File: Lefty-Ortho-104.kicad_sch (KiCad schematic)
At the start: 11 parts

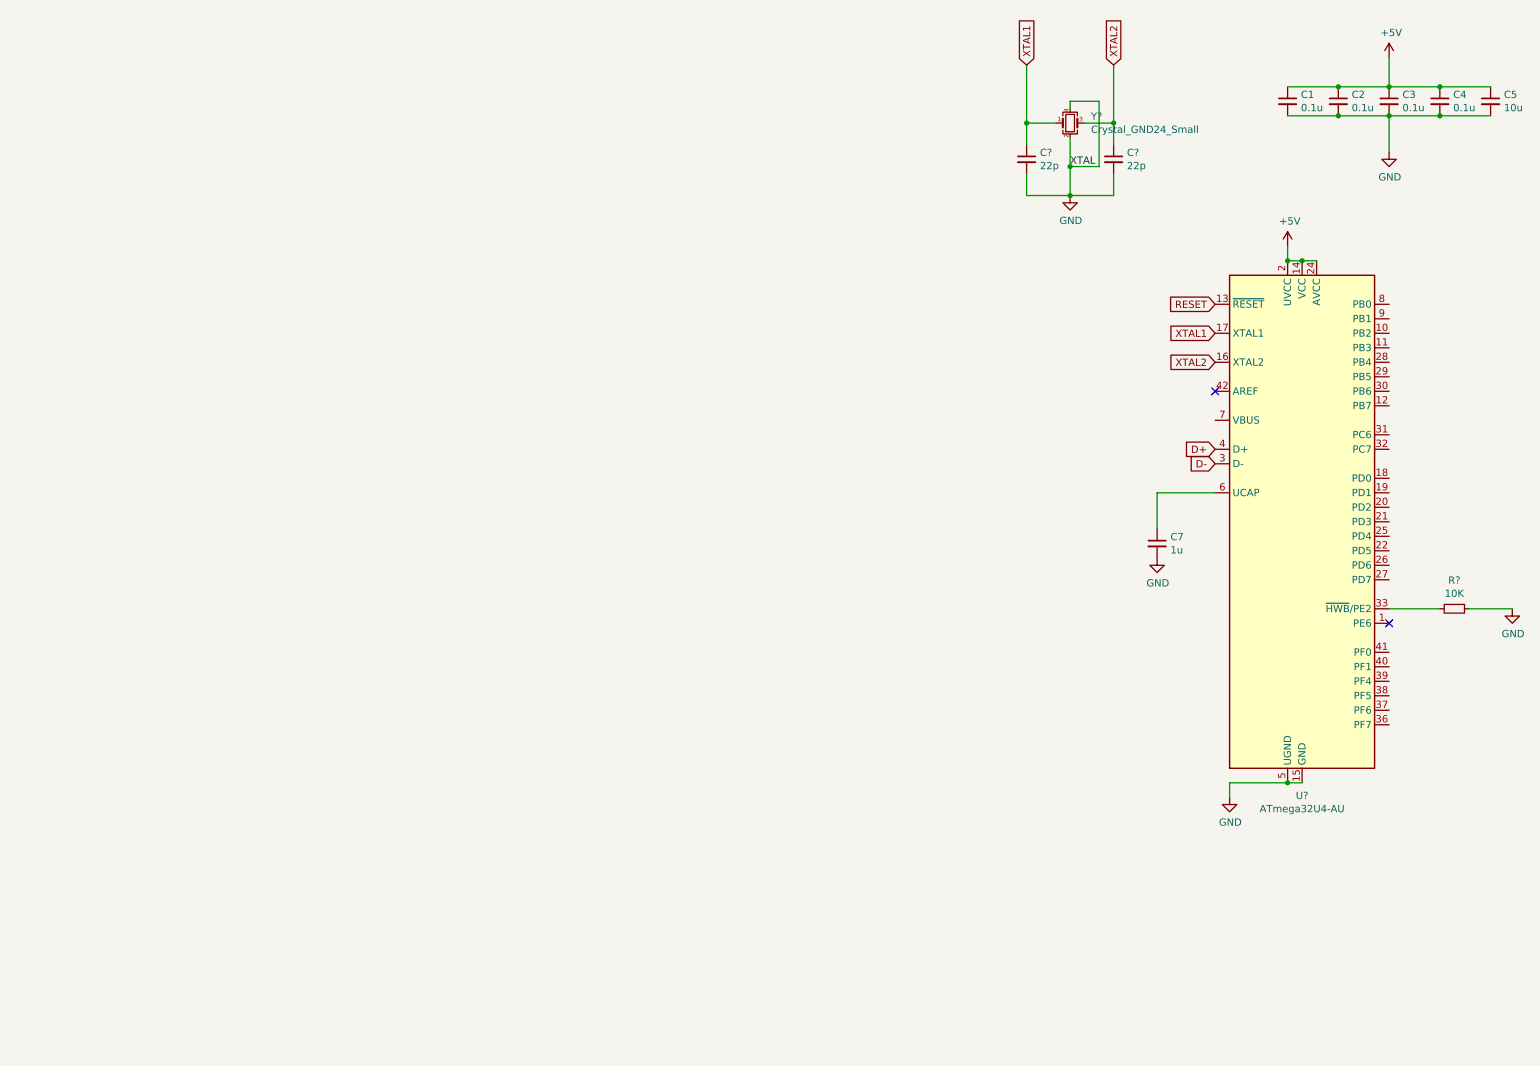
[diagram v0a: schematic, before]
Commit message: fixed ergogen files
also restarted schematic with rp2350
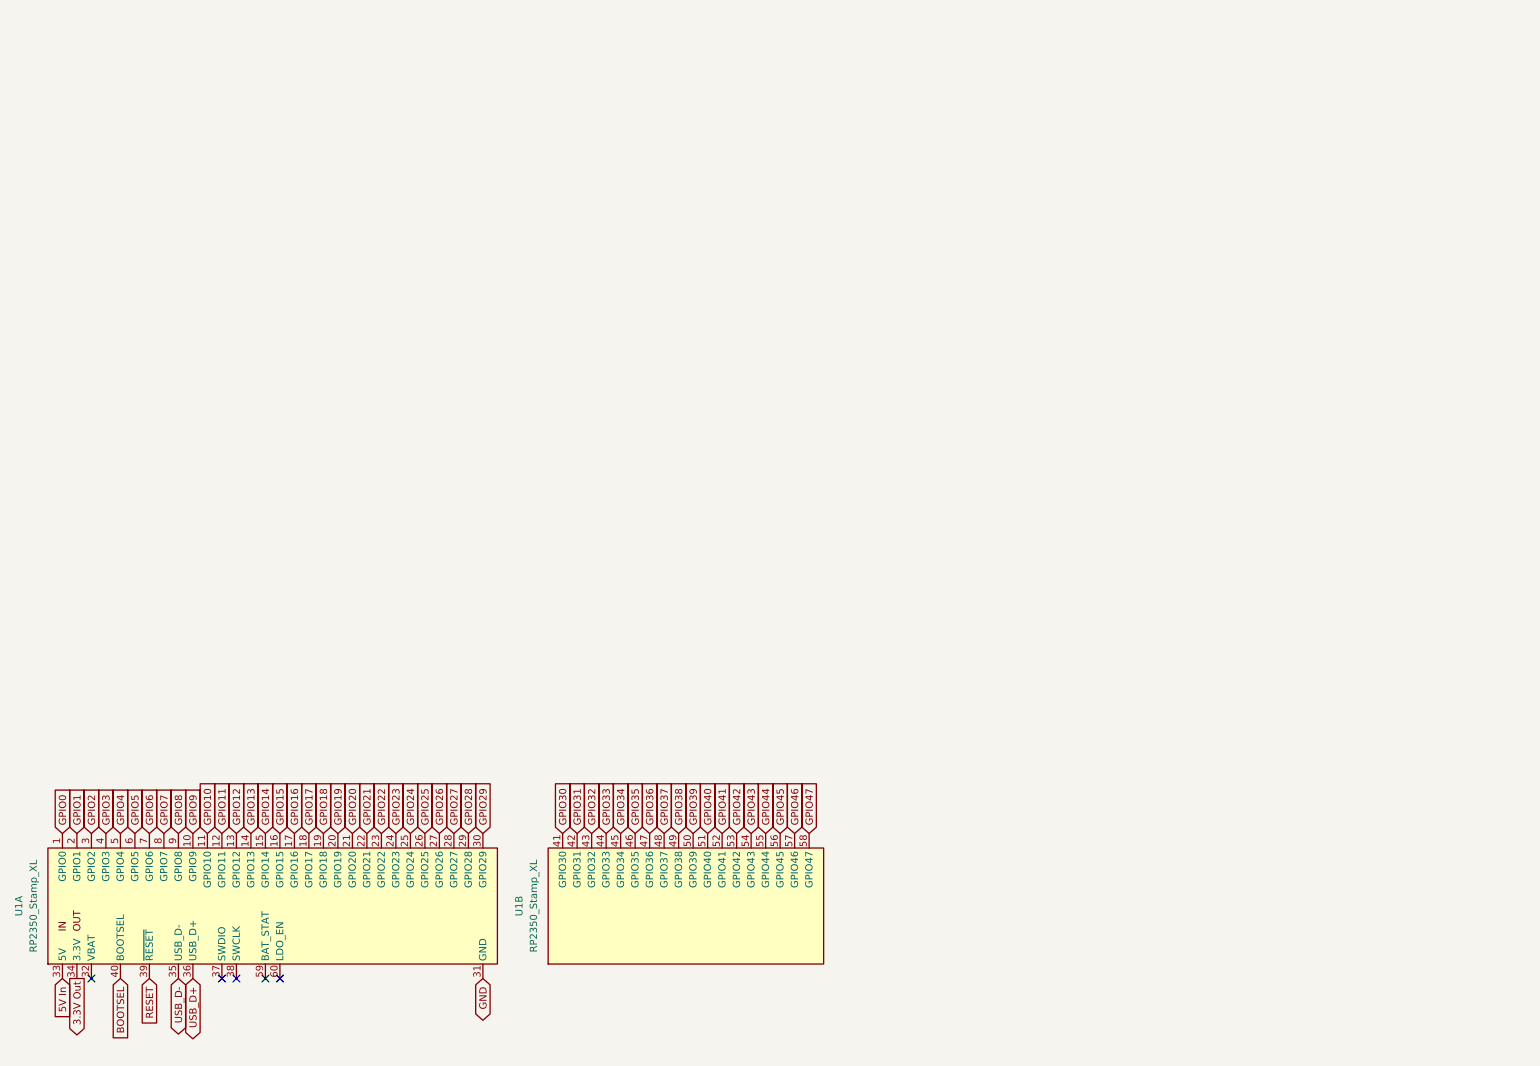
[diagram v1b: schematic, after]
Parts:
- removed C1, C2, C3, C4: 0.1u, symbol Device:C_Small
- removed C5: 10u, symbol Device:C_Small
- removed C7: 1u, symbol Device:C_Small
- removed C? (x2): 22p, symbol Device:C_Small
- removed R?: 10K, symbol Device:R_Small
- removed U?: ATmega32U4-AU, Package_QFP:TQFP-44_10x10mm_P0.8mm, symbol Lefty-Ortho-104-rescue:ATmega32U4-AU-MCU_Microchip_ATmega
- removed Y?: Crystal_GND24_Small, symbol Device:Crystal_GND24_Small
- added U1: RP2350_Stamp_XL, symbol RP2xxx_Stamp:RP2350_Stamp_XL
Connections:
- net GND: now also U1.31 (GND)
- net RESET: now also U1.39 (~{RESET})
- new net 3.3V Out: U1.34 (3.3V)
- new net 5V In: U1.33 (5V)
- new net BOOTSEL: U1.40 (BOOTSEL)
- new net GPIO0: U1.1 (GPIO0)
- new net GPIO1: U1.2 (GPIO1)
- new net GPIO10: U1.11 (GPIO10)
- new net GPIO11: U1.12 (GPIO11)
- new net GPIO12: U1.13 (GPIO12)
- new net GPIO13: U1.14 (GPIO13)
- new net GPIO14: U1.15 (GPIO14)
- new net GPIO15: U1.16 (GPIO15)
- new net GPIO16: U1.17 (GPIO16)
- new net GPIO17: U1.18 (GPIO17)
- new net GPIO18: U1.19 (GPIO18)
- new net GPIO19: U1.20 (GPIO19)
- new net GPIO2: U1.3 (GPIO2)
- new net GPIO20: U1.21 (GPIO20)
- new net GPIO21: U1.22 (GPIO21)
- new net GPIO22: U1.23 (GPIO22)
- new net GPIO23: U1.24 (GPIO23)
- new net GPIO24: U1.25 (GPIO24)
- new net GPIO25: U1.26 (GPIO25)
- new net GPIO26: U1.27 (GPIO26)
- new net GPIO27: U1.28 (GPIO27)
- new net GPIO28: U1.29 (GPIO28)
- new net GPIO29: U1.30 (GPIO29)
- new net GPIO3: U1.4 (GPIO3)
- new net GPIO30: U1.41 (GPIO30)
- new net GPIO31: U1.42 (GPIO31)
- new net GPIO32: U1.43 (GPIO32)
- new net GPIO33: U1.44 (GPIO33)
- new net GPIO34: U1.45 (GPIO34)
- new net GPIO35: U1.46 (GPIO35)
- new net GPIO36: U1.47 (GPIO36)
- new net GPIO37: U1.48 (GPIO37)
- new net GPIO38: U1.49 (GPIO38)
- new net GPIO39: U1.50 (GPIO39)
- new net GPIO4: U1.5 (GPIO4)
- new net GPIO40: U1.51 (GPIO40)
- new net GPIO41: U1.52 (GPIO41)
- new net GPIO42: U1.53 (GPIO42)
- new net GPIO43: U1.54 (GPIO43)
- new net GPIO44: U1.55 (GPIO44)
- new net GPIO45: U1.56 (GPIO45)
- new net GPIO46: U1.57 (GPIO46)
- new net GPIO47: U1.58 (GPIO47)
- new net GPIO5: U1.6 (GPIO5)
- new net GPIO6: U1.7 (GPIO6)
- new net GPIO7: U1.8 (GPIO7)
- new net GPIO8: U1.9 (GPIO8)
- new net GPIO9: U1.10 (GPIO9)
- new net USB_D+: U1.36 (USB_D+)
- new net USB_D-: U1.35 (USB_D-)
- no-connect marks 2 -> 5
